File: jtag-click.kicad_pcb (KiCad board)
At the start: 2 copper layers, 25.4 x 42.9 mm, 55 parts, among them J1 Conn_01x08, J2 Conn_01x08, J3 Conn_ARM_JTAG_SWD_20, J4 Conn_ARM_JTAG_SWD_10, Q1 2N7002W, Q2 2N7002W, U1 SN74LVC1T45DCK, U2 SN74LVC1T45DCK, U3 SN74LVC1T45DCK, U4 SN74LVC1T45DCK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

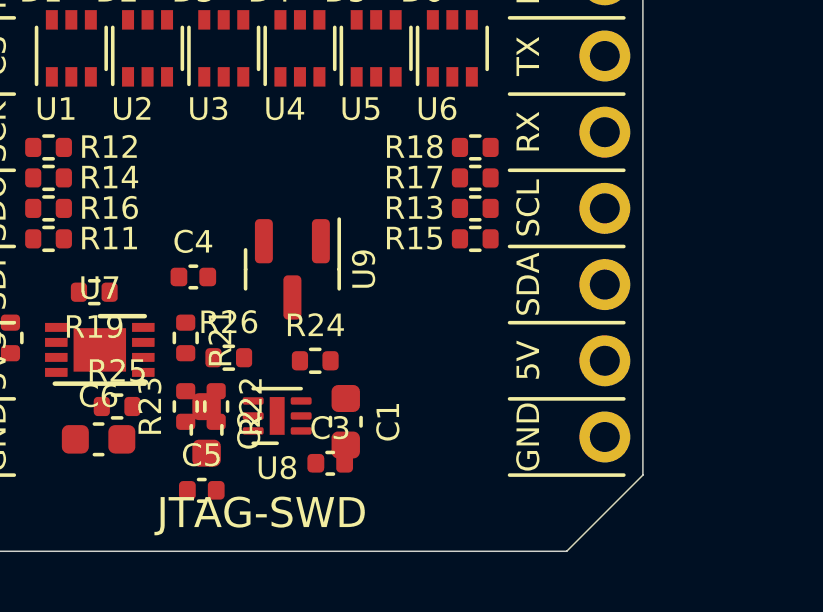
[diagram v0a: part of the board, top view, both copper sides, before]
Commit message: Add VTREF_CLICK voltage divider for sensing VTREF
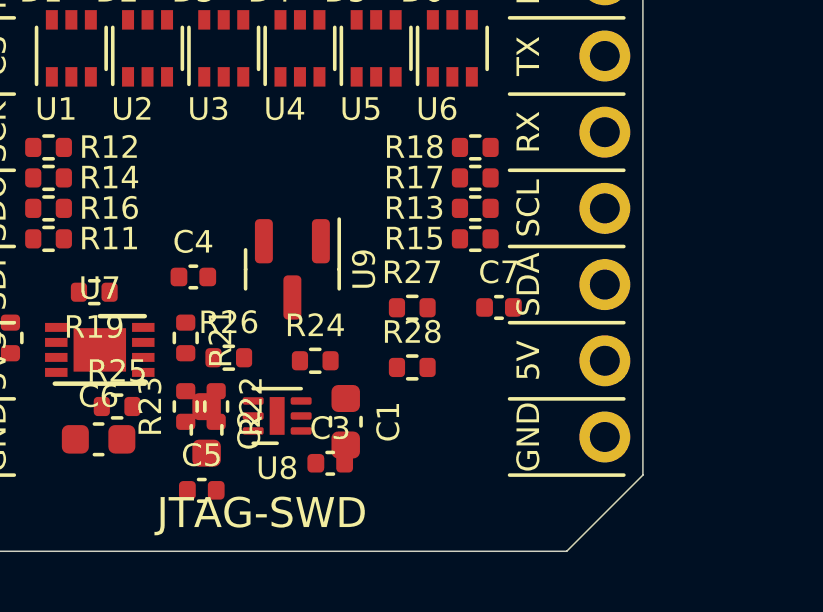
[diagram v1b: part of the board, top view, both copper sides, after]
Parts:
- added C7: 0.1uF, Capacitor_SMD:C_0402_1005Metric, F.Cu at (145.7, 116.0)
- added R27: 10.0k, Resistor_SMD:R_0402_1005Metric, F.Cu at (142.8, 116.0)
- added R28: 10.0k, Resistor_SMD:R_0402_1005Metric, F.Cu at (142.8, 118.0)
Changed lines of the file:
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@@
+    )
+  )
+  (footprint "Resistor_SMD:R_0402_1005Metric" (layer "F.Cu")
+    (at 142.812 115.977)
+    (descr "Resistor SMD 0402 (1005 Metric), square (rectangular) end terminal, IPC_7351 nominal, (Body size source: IPC-SM-782 page 72, https://www.pcb-3d.com/wordpress/wp-content/uploads/ipc-sm-782a_amendment_1_and_2.pdf), generated with kicad-footprint-generator")
+    (tags "resistor")
+    (property "Sheetfile" "jtag-click.kicad_sch")
+    (property "Sheetname" "")
+    (property "ki_description" "Resistor, US symbol")
+    (property "ki_keywords" "R res resistor")
+    (attr smd)
+    (fp_text reference "R27" (at 0 -1.17) (layer "F.SilkS")
+        (effects (font (size 0.75 0.75) (thickness 0.15)))
+    )
+    (fp_text value "10.0k" (at 0 1.17) (layer "F.Fab")
+        (effects (font (size 1 1) (thickness 0.15)))
+    )
+    (fp_text user "${REFERENCE}" (at 0 0) (layer "F.Fab")
+        (effects (font (size 0.26 0.26) (thickness 0.04)))
+    )
+    (fp_line (start -0.153641 -0.38) (end 0.153641 -0.38)
+      (stroke (width 0.12) (type solid)) (layer "F.SilkS"))
+    (fp_line (start -0.153641 0.38) (end 0.153641 0.38)
+      (stroke (width 0.12) (type solid)) (layer "F.SilkS"))
+    (fp_line (start -0.93 -0.47) (end 0.93 -0.47)
+      (stroke (width 0.05) (type solid)) (layer "F.CrtYd"))
+    (fp_line (start -0.93 0.47) (end -0.93 -0.47)
+      (stroke (width 0.05) (type solid)) (layer "F.CrtYd"))
+    (fp_line (start 0.93 -0.47) (end 0.93 0.47)
+      (stroke (width 0.05) (type solid)) (layer "F.CrtYd"))
+    (fp_line (start 0.93 0.47) (end -0.93 0.47)
+      (stroke (width 0.05) (type solid)) (layer "F.CrtYd"))
+    (fp_line (start -0.525 -0.27) (end 0.525 -0.27)
+      (stroke (width 0.1) (type solid)) (layer "F.Fab"))
+    (fp_line (start -0.525 0.27) (end -0.525 -0.27)
+      (stroke (width 0.1) (type solid)) (layer "F.Fab"))
+    (fp_line (start 0.525 -0.27) (end 0.525 0.27)
+      (stroke (width 0.1) (type solid)) (layer "F.Fab"))
+    (fp_line (start 0.525 0.27) (end -0.525 0.27)
+      (stroke (width 0.1) (type solid)) (layer "F.Fab"))
+    (pad "1" smd roundrect (at -0.51 0) (size 0.54 0.64) (layers "F.Cu" "F.Paste" "F.Mask") (roundrect_rratio 0.25)
+      (net 5 "Net-(U7A--)") (pintype "passive"))
+    (pad "2" smd roundrect (at 0.51 0) (size 0.54 0.64) (layers "F.Cu" "F.Paste" "F.Mask") (roundrect_rratio 0.25)
+      (net 9 "/VTREF_CLICK") (pintype "passive"))
+    (model "${KICAD6_3DMODEL_DIR}/Resistor_SMD.3dshapes/R_0402_1005Metric.wrl"
+      (offset (xyz 0 0 0))
+      (scale (xyz 1 1 1))
+      (rotate (xyz 0 0 0))
     )
   )
@@
       (offset (xyz 0 0 0))
       (scale (xyz 1 1 1))
+      (rotate (xyz 0 0 0))
+    )
+  )
+  (footprint "Resistor_SMD:R_0402_1005Metric" (layer "F.Cu")
+    (at 142.812 117.967)
+    (descr "Resistor SMD 0402 (1005 Metric), square (rectangular) end terminal, IPC_7351 nominal, (Body size source: IPC-SM-782 page 72, https://www.pcb-3d.com/wordpress/wp-content/uploads/ipc-sm-782a_amendment_1_and_2.pdf), generated with kicad-footprint-generator")
+    (tags "resistor")
+    (property "Sheetfile" "jtag-click.kicad_sch")
+    (property "Sheetname" "")
+    (property "ki_description" "Resistor, US symbol")
+    (property "ki_keywords" "R res resistor")
+    (attr smd)
+    (fp_text reference "R28" (at 0 -1.17) (layer "F.SilkS")
+        (effects (font (size 0.75 0.75) (thickness 0.15)))
+    )
+    (fp_text value "10.0k" (at 0 1.17) (layer "F.Fab")
+        (effects (font (size 1 1) (thickness 0.15)))
+    )
+    (fp_text user "${REFERENCE}" (at 0 0) (layer "F.Fab")
+        (effects (font (size 0.26 0.26) (thickness 0.04)))
+    )
+    (fp_line (start -0.153641 -0.38) (end 0.153641 -0.38)
+      (stroke (width 0.12) (type solid)) (layer "F.SilkS"))
+    (fp_line (start -0.153641 0.38) (end 0.153641 0.38)
+      (stroke (width 0.12) (type solid)) (layer "F.SilkS"))
+    (fp_line (start -0.93 -0.47) (end 0.93 -0.47)
+      (stroke (width 0.05) (type solid)) (layer "F.CrtYd"))
+    (fp_line (start -0.93 0.47) (end -0.93 -0.47)
+      (stroke (width 0.05) (type solid)) (layer "F.CrtYd"))
+    (fp_line (start 0.93 -0.47) (end 0.93 0.47)
+      (stroke (width 0.05) (type solid)) (layer "F.CrtYd"))
+    (fp_line (start 0.93 0.47) (end -0.93 0.47)
+      (stroke (width 0.05) (type solid)) (layer "F.CrtYd"))
+    (fp_line (start -0.525 -0.27) (end 0.525 -0.27)
+      (stroke (width 0.1) (type solid)) (layer "F.Fab"))
+    (fp_line (start -0.525 0.27) (end -0.525 -0.27)
+      (stroke (width 0.1) (type solid)) (layer "F.Fab"))
+    (fp_line (start 0.525 -0.27) (end 0.525 0.27)
+      (stroke (width 0.1) (type solid)) (layer "F.Fab"))
+    (fp_line (start 0.525 0.27) (end -0.525 0.27)
+      (stroke (width 0.1) (type solid)) (layer "F.Fab"))
+    (pad "1" smd roundrect (at -0.51 0) (size 0.54 0.64) (layers "F.Cu" "F.Paste" "F.Mask") (roundrect_rratio 0.25)
+      (net 9 "/VTREF_CLICK") (pintype "passive"))
+    (pad "2" smd roundrect (at 0.51 0) (size 0.54 0.64) (layers "F.Cu" "F.Paste" "F.Mask") (roundrect_rratio 0.25)
+      (net 2 "GND") (pintype "passive"))
+    (model "${KICAD6_3DMODEL_DIR}/Resistor_SMD.3dshapes/R_0402_1005Metric.wrl"
+      (offset (xyz 0 0 0))
+      (scale (xyz 1 1 1))
+      (rotate (xyz 0 0 0))
+    )
+  )
+  (footprint "Capacitor_SMD:C_0402_1005Metric" (layer "F.Cu")
+    (at 145.702 115.967)
+    (descr "Capacitor SMD 0402 (1005 Metric), square (rectangular) end terminal, IPC_7351 nominal, (Body size source: IPC-SM-782 page 76, https://www.pcb-3d.com/wordpress/wp-content/uploads/ipc-sm-782a_amendment_1_and_2.pdf), generated with kicad-footprint-generator")
+    (tags "capacitor")
+    (property "Sheetfile" "jtag-click.kicad_sch")
+    (property "Sheetname" "")
+    (property "ki_description" "Unpolarized capacitor")
+    (property "ki_keywords" "cap capacitor")
+    (attr smd)
+    (fp_text reference "C7" (at 0 -1.16) (layer "F.SilkS")
+        (effects (font (size 0.75 0.75) (thickness 0.15)))
+    )
+    (fp_text value "0.1uF" (at 0 1.16) (layer "F.Fab")
+        (effects (font (size 1 1) (thickness 0.15)))
+    )
+    (fp_text user "${REFERENCE}" (at 0 0) (layer "F.Fab")
+        (effects (font (size 0.25 0.25) (thickness 0.04)))
+    )
+    (fp_line (start -0.107836 -0.36) (end 0.107836 -0.36)
+      (stroke (width 0.12) (type solid)) (layer "F.SilkS"))
+    (fp_line (start -0.107836 0.36) (end 0.107836 0.36)
+      (stroke (width 0.12) (type solid)) (layer "F.SilkS"))
+    (fp_line (start -0.91 -0.46) (end 0.91 -0.46)
+      (stroke (width 0.05) (type solid)) (layer "F.CrtYd"))
+    (fp_line (start -0.91 0.46) (end -0.91 -0.46)
+      (stroke (width 0.05) (type solid)) (layer "F.CrtYd"))
+    (fp_line (start 0.91 -0.46) (end 0.91 0.46)
+      (stroke (width 0.05) (type solid)) (layer "F.CrtYd"))
+    (fp_line (start 0.91 0.46) (end -0.91 0.46)
+      (stroke (width 0.05) (type solid)) (layer "F.CrtYd"))
+    (fp_line (start -0.5 -0.25) (end 0.5 -0.25)
+      (stroke (width 0.1) (type solid)) (layer "F.Fab"))
+    (fp_line (start -0.5 0.25) (end -0.5 -0.25)
+      (stroke (width 0.1) (type solid)) (layer "F.Fab"))
+    (fp_line (start 0.5 -0.25) (end 0.5 0.25)
+      (stroke (width 0.1) (type solid)) (layer "F.Fab"))
+    (fp_line (start 0.5 0.25) (end -0.5 0.25)
+      (stroke (width 0.1) (type solid)) (layer "F.Fab"))
+    (pad "1" smd roundrect (at -0.48 0) (size 0.56 0.62) (layers "F.Cu" "F.Paste" "F.Mask") (roundrect_rratio 0.25)
+      (net 9 "/VTREF_CLICK") (pintype "passive"))
+    (pad "2" smd roundrect (at 0.48 0) (size 0.56 0.62) (layers "F.Cu" "F.Paste" "F.Mask") (roundrect_rratio 0.25)
+      (net 2 "GND") (pintype "passive"))
+    (model "${KICAD6_3DMODEL_DIR}/Capacitor_SMD.3dshapes/C_0402_1005Metric.wrl"
+      (offset (xyz 0 0 0))
+      (scale (xyz 1 1 1))

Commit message: Change Vp of clamp diodes to 5V to prevent current flow if VDD is disabled.
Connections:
- D1 pad 2: VDD -> +5V
- D2 pad 2: VDD -> +5V
- D3 pad 2: VDD -> +5V
- D4 pad 2: VDD -> +5V
- D5 pad 2: VDD -> +5V
- D6 pad 2: VDD -> +5V
- D7 pad 2: VDD -> +5V
- D8 pad 2: VDD -> +5V
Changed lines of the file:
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@@
       (net 43 "Net-(D7-common)") (pinfunction "common") (pintype "passive"))
     (pad "2" smd rect (at -1 0.65 180) (size 0.45 0.7) (layers "F.Cu" "F.Paste" "F.Mask")
-      (net 8 "VDD") (pinfunction "K") (pintype "passive"))
+      (net 3 "+5V") (pinfunction "K") (pintype "passive"))
     (pad "3" smd rect (at 1 0 180) (size 0.45 0.7) (layers "F.Cu" "F.Paste" "F.Mask")
       (net 2 "GND") (pinfunction "A") (pintype "passive"))
@@
       (net 44 "Net-(D8-common)") (pinfunction "common") (pintype "passive"))
     (pad "2" smd rect (at -1 0.65 180) (size 0.45 0.7) (layers "F.Cu" "F.Paste" "F.Mask")
-      (net 8 "VDD") (pinfunction "K") (pintype "passive"))
+      (net 3 "+5V") (pinfunction "K") (pintype "passive"))
     (pad "3" smd rect (at 1 0 180) (size 0.45 0.7) (layers "F.Cu" "F.Paste" "F.Mask")
       (net 2 "GND") (pinfunction "A") (pintype "passive"))
@@
       (net 41 "Net-(D5-common)") (pinfunction "common") (pintype "passive"))
     (pad "2" smd rect (at -1 0.65 180) (size 0.45 0.7) (layers "F.Cu" "F.Paste" "F.Mask")
-      (net 8 "VDD") (pinfunction "K") (pintype "passive"))
+      (net 3 "+5V") (pinfunction "K") (pintype "passive"))
     (pad "3" smd rect (at 1 0 180) (size 0.45 0.7) (layers "F.Cu" "F.Paste" "F.Mask")
       (net 2 "GND") (pinfunction "A") (pintype "passive"))
@@
       (net 42 "Net-(D6-common)") (pinfunction "common") (pintype "passive"))
     (pad "2" smd rect (at -1 0.65 180) (size 0.45 0.7) (layers "F.Cu" "F.Paste" "F.Mask")
-      (net 8 "VDD") (pinfunction "K") (pintype "passive"))
+      (net 3 "+5V") (pinfunction "K") (pintype "passive"))
     (pad "3" smd rect (at 1 0 180) (size 0.45 0.7) (layers "F.Cu" "F.Paste" "F.Mask")
       (net 2 "GND") (pinfunction "A") (pintype "passive"))
@@
       (net 40 "Net-(D4-common)") (pinfunction "common") (pintype "passive"))
     (pad "2" smd rect (at -1 0.65 180) (size 0.45 0.7) (layers "F.Cu" "F.Paste" "F.Mask")
-      (net 8 "VDD") (pinfunction "K") (pintype "passive"))
+      (net 3 "+5V") (pinfunction "K") (pintype "passive"))
     (pad "3" smd rect (at 1 0 180) (size 0.45 0.7) (layers "F.Cu" "F.Paste" "F.Mask")
       (net 2 "GND") (pinfunction "A") (pintype "passive"))
@@
       (net 39 "Net-(D3-common)") (pinfunction "common") (pintype "passive"))
     (pad "2" smd rect (at -1 0.65 180) (size 0.45 0.7) (layers "F.Cu" "F.Paste" "F.Mask")
-      (net 8 "VDD") (pinfunction "K") (pintype "passive"))
+      (net 3 "+5V") (pinfunction "K") (pintype "passive"))
     (pad "3" smd rect (at 1 0 180) (size 0.45 0.7) (layers "F.Cu" "F.Paste" "F.Mask")
       (net 2 "GND") (pinfunction "A") (pintype "passive"))
@@
       (net 37 "Net-(D1-common)") (pinfunction "common") (pintype "passive"))
     (pad "2" smd rect (at -1 0.65 180) (size 0.45 0.7) (layers "F.Cu" "F.Paste" "F.Mask")
-      (net 8 "VDD") (pinfunction "K") (pintype "passive"))
+      (net 3 "+5V") (pinfunction "K") (pintype "passive"))
     (pad "3" smd rect (at 1 0 180) (size 0.45 0.7) (layers "F.Cu" "F.Paste" "F.Mask")
       (net 2 "GND") (pinfunction "A") (pintype "passive"))
@@
       (net 38 "Net-(D2-common)") (pinfunction "common") (pintype "passive"))
     (pad "2" smd rect (at -1 0.65 180) (size 0.45 0.7) (layers "F.Cu" "F.Paste" "F.Mask")
-      (net 8 "VDD") (pinfunction "K") (pintype "passive"))
+      (net 3 "+5V") (pinfunction "K") (pintype "passive"))
     (pad "3" smd rect (at 1 0 180) (size 0.45 0.7) (layers "F.Cu" "F.Paste" "F.Mask")
       (net 2 "GND") (pinfunction "A") (pintype "passive"))
